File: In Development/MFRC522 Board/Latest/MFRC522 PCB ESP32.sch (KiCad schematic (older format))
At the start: 50 parts, among them P1 ESP32 DEVKIT1 LEFT HEADER-MAL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, P2 ESP32 DEVKIT1 RIGHT HEADER-MA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, Q2 Q_NPN_BEC, U1 MFRC522, Y1 27.12 MHz

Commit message: update all files
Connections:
- net GND: now also U1.1 (I2C)
- no-connect marks 27 -> 26
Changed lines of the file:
@@
 NoConn ~ 4400 3900
 NoConn ~ 4100 3600
-NoConn ~ 4100 2900
 NoConn ~ 4100 3500
 Text HLabel 4500 2000 1    50   BiDi ~ 0
@@
 Text Notes 8150 7650 0    50   ~ 0
 02/06/2022\n
+$Comp
+L power:GND #PWR?
+U 1 1 628873A7
+P 3800 2700
+F 0 "#PWR?" H 3800 2450 50  0001 C CNN
+F 1 "GND" H 3805 2527 50  0000 C CNN
+F 2 "" H 3800 2700 50  0001 C CNN
+F 3 "" H 3800 2700 50  0001 C CNN
+	1    3800 2700
+	1    0    0    -1
+$EndComp
+Wire Wire Line
+	4100 2900 3950 2900
+Wire Wire Line
+	3950 2900 3950 2650
+Wire Wire Line
+	3950 2650 3800 2650
+Wire Wire Line
+	3800 2650 3800 2700
 $EndSCHEMATC

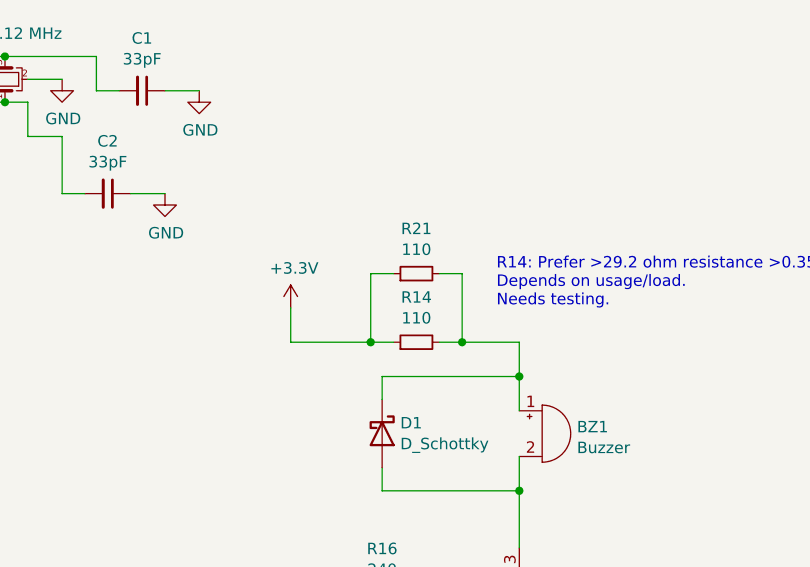
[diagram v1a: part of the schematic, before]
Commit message: rm buzzer resistors add lettering to back
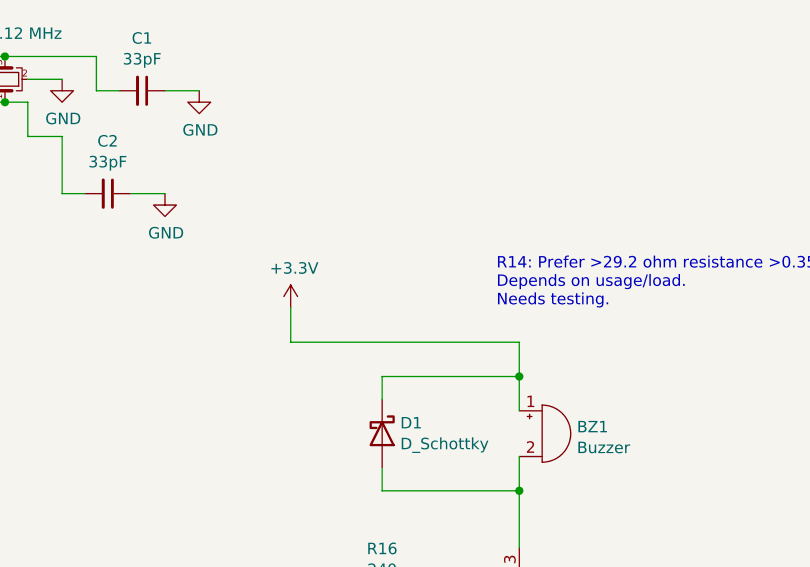
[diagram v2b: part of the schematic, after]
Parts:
- removed R14, R21: 110, Resistor_SMD:R_0805_2012Metric, symbol Device:R_Small
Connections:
- net +3V3: now also BZ1.1 (-), D1.1 (K)
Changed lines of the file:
@@
 	0    -1   -1   0
 $EndComp
-$Comp
-L Device:R_Small R14
-U 1 1 5EF0556E
-P 8350 4450
-F 0 "R14" V 8546 4450 50  0000 C CNN
-F 1 "110" V 8455 4450 50  0000 C CNN
-F 2 "Resistor_SMD:R_0805_2012Metric" H 8350 4450 50  0001 C CNN
-F 3 "~" H 8350 4450 50  0001 C CNN
-	1    8350 4450
-	0    -1   -1   0
-$EndComp
-Wire Wire Line
-	7800 4450 8150 4450
-Wire Wire Line
-	8450 4450 8550 4450
 Wire Wire Line
 	8800 4950 8800 5100
@@
 	1    0    0    -1
 $EndComp
-Connection ~ 8150 4450
-Wire Wire Line
-	8150 4450 8250 4450
-Connection ~ 8550 4450
-Wire Wire Line
-	8550 4450 8800 4450
 NoConn ~ 1650 3600
 NoConn ~ 1650 3900
@@
 	3000 6350 3000 6450
 $Comp
-L Device:R_Small R21
-U 1 1 6095FA2D
-P 8350 4150
-F 0 "R21" V 8546 4150 50  0000 C CNN
-F 1 "110" V 8455 4150 50  0000 C CNN
-F 2 "Resistor_SMD:R_0805_2012Metric" H 8350 4150 50  0001 C CNN
-F 3 "~" H 8350 4150 50  0001 C CNN
-	1    8350 4150
-	0    -1   -1   0
-$EndComp
-Wire Wire Line
-	8450 4150 8550 4150
-Wire Wire Line
-	8550 4150 8550 4450
-Wire Wire Line
-	8250 4150 8150 4150
-Wire Wire Line
-	8150 4150 8150 4450
-$Comp
 L power:+3.3V #PWR0125
 U 1 1 608A03BF
@@
 Wire Wire Line
 	3800 2650 3800 2700
+Wire Wire Line
+	7800 4450 8800 4450
 $EndSCHEMATC
